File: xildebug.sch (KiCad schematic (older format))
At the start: 37 parts, among them J1 USB_B_Micro, J2 Conn_STM_SWD, J3 Conn_Ext1, J4 Conn_Ext2, J5 Conn_DUT, J6 Conn_DUT_VDD, U1 XC6206P332MR, U2 MAX14662, U3 STM32L433CCUx

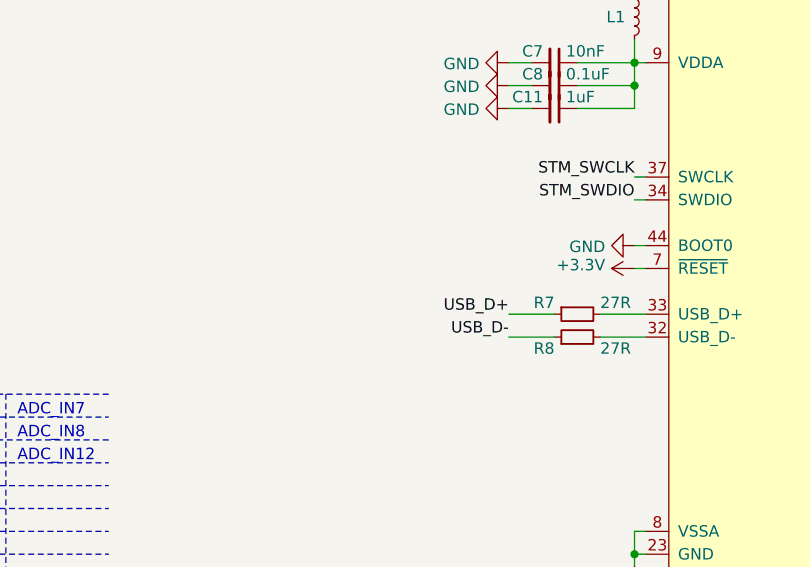
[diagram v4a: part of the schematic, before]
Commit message: Add button on BOOT0
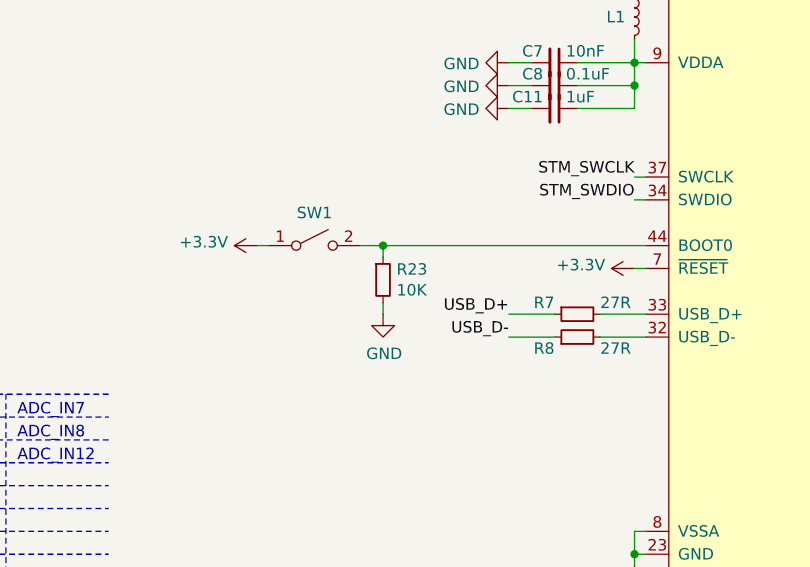
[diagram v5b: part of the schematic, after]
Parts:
- added R23: 10K, Resistor_SMD:R_0603_1608Metric, symbol Device:R_Small
- added SW1: BOOT0, Button_Switch_SMD:SW_SPST_B3U-1000P, symbol Switch:SW_SPST
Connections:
- net +3V3: now also SW1.1 (A)
- net GND: now also R23.2; no longer U3.44 (BOOT0)
- new net: R23.1, SW1.2 (B), U3.44 (BOOT0)
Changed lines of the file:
@@
 Connection ~ 5200 5550
-Wire Wire Line
-	5250 4200 5200 4200
 Wire Wire Line
 	5250 4300 5200 4300
@@
 Wire Wire Line
 	6100 1000 6350 1000
-$Comp
-L power:GND #PWR0101
-U 1 1 5BB12C8D
-P 5200 4200
-F 0 "#PWR0101" H 5200 3950 50  0001 C CNN
-F 1 "GND" V 5205 4072 50  0000 R CNN
-F 2 "" H 5200 4200 50  0001 C CNN
-F 3 "" H 5200 4200 50  0001 C CNN
-	1    5200 4200
-	0    1    1    0
-$EndComp
 Text Notes 9550 3800 2    50   ~ 0
 I2C: 0x98
@@
 Wire Wire Line
 	10000 3700 9950 3700
+Wire Wire Line
+	4000 4200 4100 4200
+$Comp
+L power:GND #PWR0101
+U 1 1 5BEB6345
+P 4100 4500
+F 0 "#PWR0101" H 4100 4250 50  0001 C CNN
+F 1 "GND" H 4105 4327 50  0000 C CNN
+F 2 "" H 4100 4500 50  0001 C CNN
+F 3 "" H 4100 4500 50  0001 C CNN
+	1    4100 4500
+	1    0    0    -1
+$EndComp
+Wire Wire Line
+	4100 4500 4100 4450
+Wire Wire Line
+	4100 4200 4100 4250
+Connection ~ 4100 4200
+Wire Wire Line
+	4100 4200 5250 4200
+$Comp
+L Device:R_Small R23
+U 1 1 5BED7253
+P 4100 4350
+F 0 "R23" H 4159 4396 50  0000 L CNN
+F 1 "10K" H 4159 4305 50  0000 L CNN
+F 2 "Resistor_SMD:R_0603_1608Metric" H 4100 4350 50  0001 C CNN
+F 3 "~" H 4100 4350 50  0001 C CNN
+	1    4100 4350
+	1    0    0    -1
+$EndComp
+$Comp
+L power:+3.3V #PWR0102
+U 1 1 5BEE7F28
+P 3550 4200
+F 0 "#PWR0102" H 3550 4050 50  0001 C CNN
+F 1 "+3.3V" V 3565 4328 50  0000 L CNN
+F 2 "" H 3550 4200 50  0001 C CNN
+F 3 "" H 3550 4200 50  0001 C CNN
+	1    3550 4200
+	0    -1   -1   0
+$EndComp
+Wire Wire Line
+	3550 4200 3600 4200
+$Comp
+L Switch:SW_SPST SW1
+U 1 1 5BEF9165
+P 3800 4200
+F 0 "SW1" H 3800 4343 50  0000 C CNN
+F 1 "BOOT0" H 3800 4344 50  0001 C CNN
+F 2 "Button_Switch_SMD:SW_SPST_B3U-1000P" H 3800 4200 50  0001 C CNN
+F 3 "" H 3800 4200 50  0001 C CNN
+	1    3800 4200
+	1    0    0    -1
+$EndComp
 $EndSCHEMATC

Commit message: Minification
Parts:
- removed C11: 1uF, Capacitor_SMD:C_0603_1608Metric, symbol Device:C_Small
- removed C8: 0.1uF, Capacitor_SMD:C_0603_1608Metric, symbol Device:C_Small
- removed D4: LED_RGB, LED_SMD_Extra:LED_RGB_0606_1616Metric, symbol Device_Extra:LED_GRAB
- removed J3: Conn_Ext1, Connector_PinHeader_2.54mm:PinHeader_1x11_P2.54mm_Vertical, symbol Connector_Generic:Conn_01x11
- removed J4: Conn_Ext2, Connector_PinHeader_2.54mm:PinHeader_1x12_P2.54mm_Vertical, symbol Connector_Generic:Conn_01x12
- removed J6: Conn_DUT_VDD, Connector_PinHeader_2.54mm:PinHeader_1x03_P2.54mm_Horizontal, symbol Connector_Generic:Conn_01x03
- removed L1: FB, Inductor_SMD:L_0603_1608Metric, symbol Device:L_Small
- removed R4, R5, R6: 360R, Resistor_SMD:R_0603_1608Metric, symbol Device:R_Small
- added J3: Conn_GPIO, Connector_PinHeader_2.54mm:PinHeader_1x04_P2.54mm_Vertical, symbol Connector_Generic:Conn_01x04
- added Q?: FDN340P, Package_TO_SOT_SMD:SOT-23, symbol Transistor_FET:BSS84
- J1: symbol Connector_Specialized:USB_B_Micro -> xildebug-rescue:USB_B_Micro-Connector_Specialized
- J2: footprint Connector_PinHeader_2.54mm:PinHeader_1x04_P2.54mm_Vertical -> Connector_JST:JST_SH_BM04B-SRSS-TB_1x04-1MP_P1.00mm_Vertical
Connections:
- net DUT_VDD_EN is gone; now on net DUT_UART_RX_LED: U3.18 (PB0)
- net PA2 is gone; now on net DUT_UART_TX_A: U3.12 (PA2)
- net PA3 is gone; now on net DUT_UART_RX_A: U3.13 (PA3)
- net PA7 is gone; now on net DUT_UART_TX_LED: U3.17 (PA7)
- net PC15 is gone; now on net GPIO1_A: U3.4 (PC15)
- net SHUNT1_EN is gone; now on net DUT_SWCLK_A: U3.15 (PA5)
- net +3V3: now also C7.1, U3.9 (VDDA), Q?.3 (D)
- net DUT_SWCLK_A: now also U2.2 (A1); no longer U2.5 (A4), U3.19 (PB1)
- net DUT_SWCLK_B: now also U2.21 (B1); no longer U2.18 (B4)
- net DUT_SWDIO_A: now also U3.14 (PA4); no longer U3.20 (PB2)
- net DUT_SWD_LED: now also U3.19 (PB1); no longer U3.14 (PA4)
- net DUT_UART_RX_A: now also U2.5 (A4); no longer U2.2 (A1), U3.22 (PB11)
- net DUT_UART_RX_B: now also D5.2 (A); no longer D6.2 (A)
- net DUT_UART_RX_LED: no longer U3.6 (PH1)
- net DUT_UART_TX_A: no longer U3.21 (PB10)
- net DUT_UART_TX_B: now also D6.1 (K); no longer D5.1 (K)
- net DUT_UART_TX_LED: no longer U3.5 (PH0)
- net GPIO0_A: now also U3.3 (PC14); no longer U3.45 (PB8)
- net GPIO0_B: now also J3.1 (Pin_1)
- net GPIO1_A: no longer U3.46 (PB9)
- net GPIO1_B: now also J3.2 (Pin_2)
- net GPIO2_A: now also U3.5 (PH0); no longer U3.2 (PC13)
- net GPIO2_B: now also J3.3 (Pin_3)
- net GPIO3_A: now also U3.6 (PH1); no longer U3.3 (PC14)
- net GPIO3_B: now also J3.4 (Pin_4)
- net at U2.20 (B2): now also D6.2 (A); no longer D5.2 (A)
- net DUT_VDD_IN_DIV: no longer names the net of U3.10 (PA0)
- net DUT_VDD_OUT: no longer names the net of J5.1 (Pin_1)
- net DUT_VDD_OUT: now also Q?.2 (S)
- net DUT_VDD_OUT_DIV: no longer names the net of U3.11 (PA1)
- net LED_RGB_B: no longer names the net of U3.25 (PB12)
- net LED_RGB_G: no longer names the net of U3.29 (PA8)
- net LED_RGB_R: no longer names the net of U3.38 (PA15)
- net PB13: no longer names the net of U3.26 (PB13)
- net PB14: no longer names the net of U3.27 (PB14)
- net PB15: no longer names the net of U3.28 (PB15)
- net PB3: no longer names the net of U3.39 (PB3)
- net PB4: no longer names the net of U3.40 (PB4)
- net PB5: no longer names the net of U3.41 (PB5)
- net PB6: no longer names the net of U3.42 (PB6)
- net PB7: no longer names the net of U3.43 (PB7)
- net POT_SCL renamed STM_SCL
- net POT_SDA renamed STM_SDA
- net SHUNT2_EN renamed DUT_VDD_CTRL
- net DUT_VDD_CTRL: now also Q?.1 (G)
- new net: D5.1 (K), U2.18 (B4)
- no-connect marks 1 -> 20
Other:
- note removed: "TODO:\n- Quadruple check pinouts and footprints\n- Check USB detection circuit"
- moved on the sheet: D5, D6, J2, J5, R9

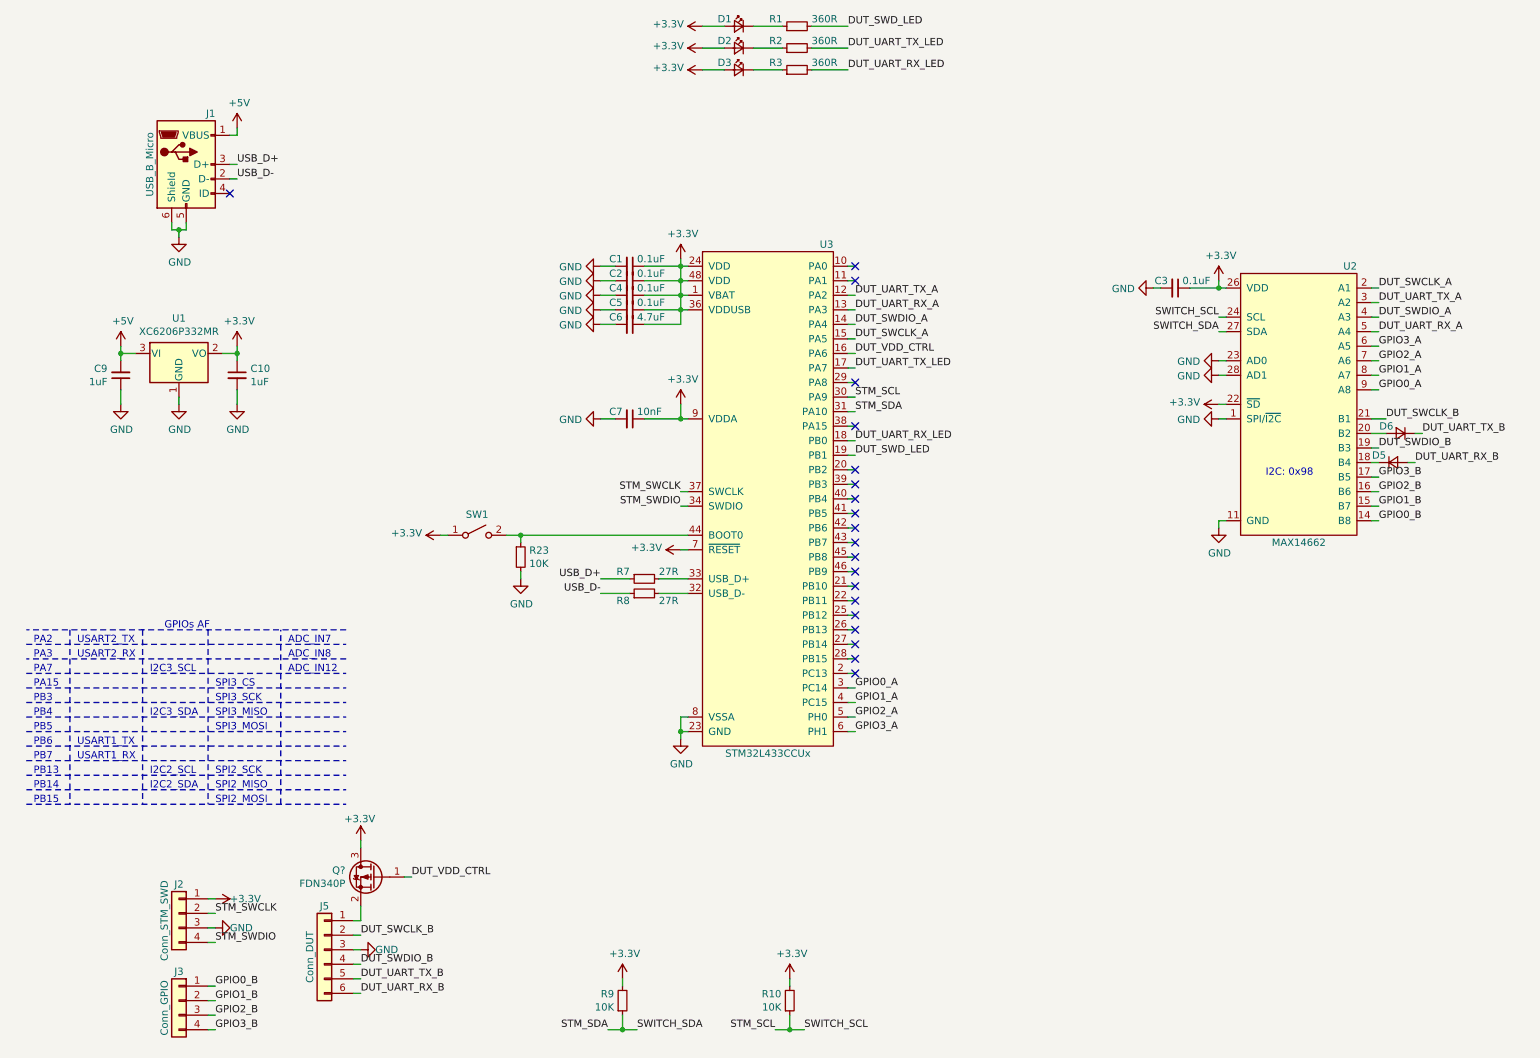
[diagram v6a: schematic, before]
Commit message: rev2
- Replaced the VDD mosfet with a analog switch
- Changed footprint of STM32L433 to standard one
- Moved UART to USART3, same as xildebug big
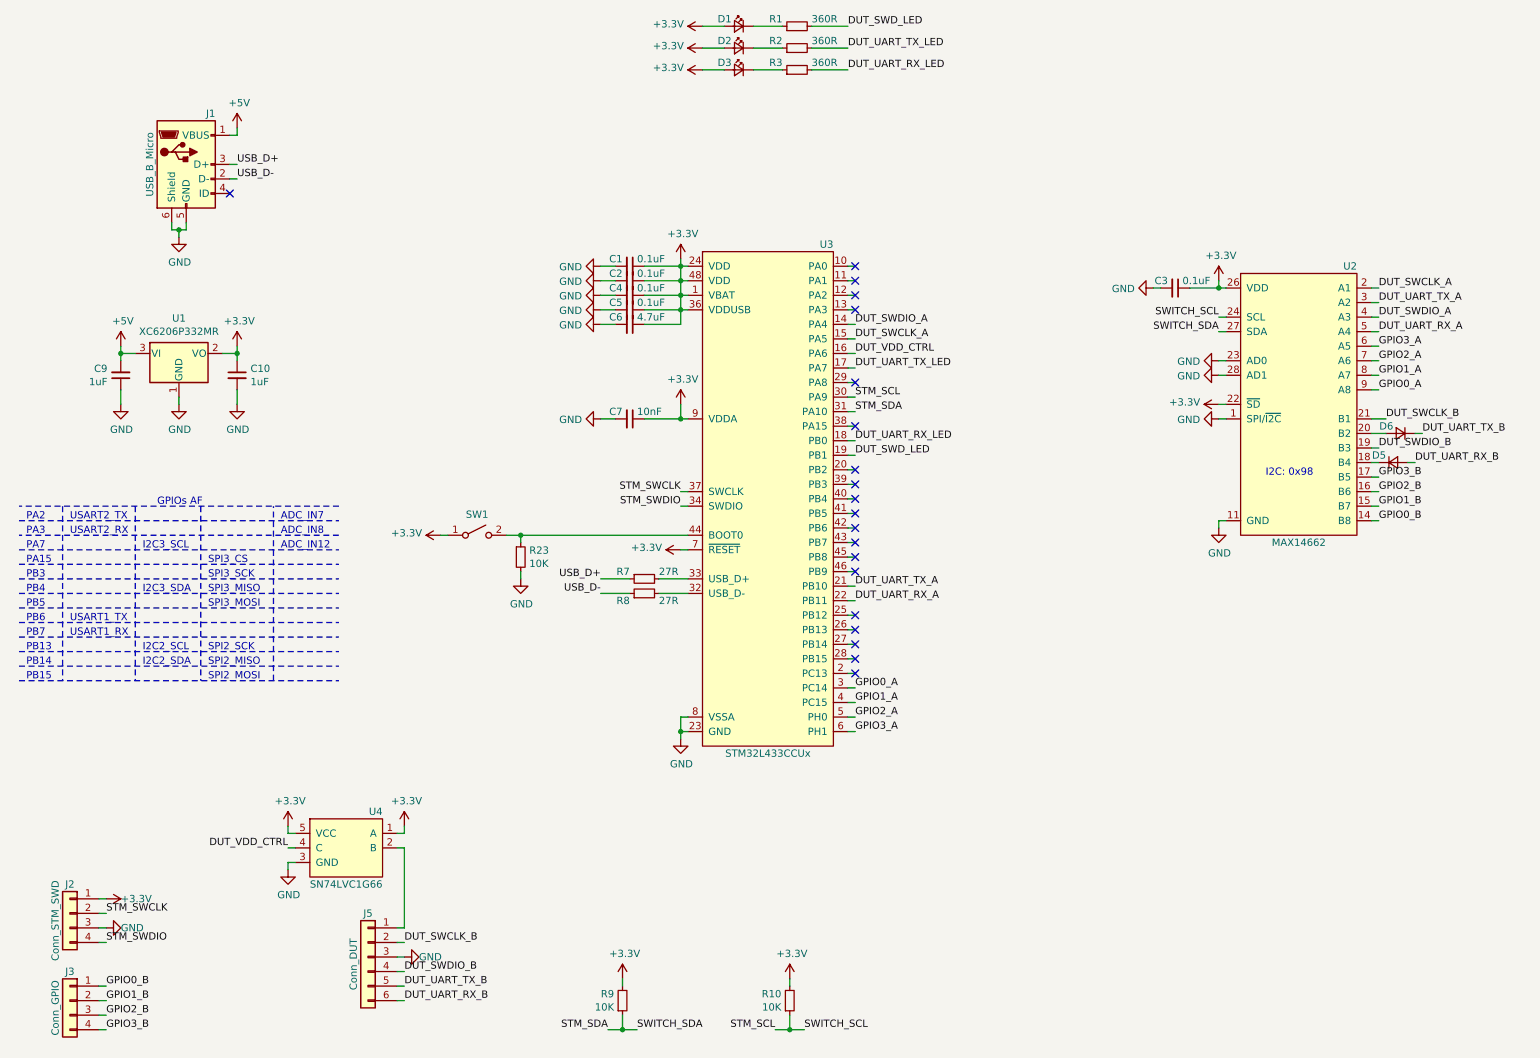
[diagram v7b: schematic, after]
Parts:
- removed Q?: FDN340P, Package_TO_SOT_SMD:SOT-23, symbol Transistor_FET:BSS84
- added U4: SN74LVC1G66, Package_TO_SOT_SMD_Extra:SC-70-5, symbol Analog_Switch_Extra:SN74LVC1G66
- U3: footprint Package_DFN_QFN_Extra:UFQFPN-48-1EP_7x7mm_P0.5mm_EP5.15x5.15mm -> Package_DFN_QFN:QFN-48-1EP_7x7mm_P0.5mm_EP5.15x5.15mm
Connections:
- net +3V3: now also U4.1 (A), U4.5 (VCC)
- net DUT_UART_RX_A: now also U3.22 (PB11); no longer U3.13 (PA3)
- net DUT_UART_TX_A: now also U3.21 (PB10); no longer U3.12 (PA2)
- net DUT_VDD_CTRL: now also U4.4 (C)
- net GND: now also U4.3 (GND)
- net at J5.1 (Pin_1): now also U4.2 (B)
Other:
- moved on the sheet: J2, J3, J5
